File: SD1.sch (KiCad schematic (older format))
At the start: 32 parts, among them J107 FPC PMS, Q101 BSS138, Q102 PDTC114EU,115, SW103 Multidirection_Switch, SW104 Multifunction_Switch, U101 TLV70233_SOT23-5, U102 ER-TFTM028-4, U104 CC2652P, U107 MCP23017

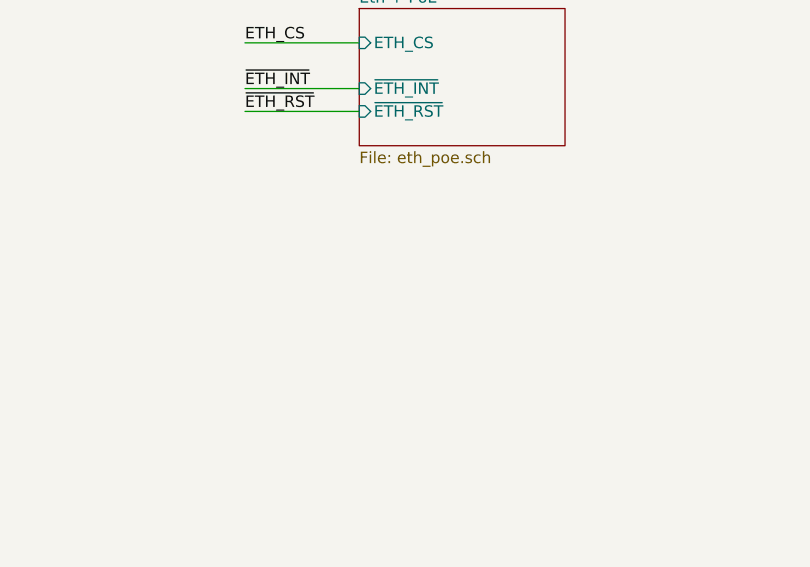
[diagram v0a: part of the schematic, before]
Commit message: Boilerplate for CO sensor
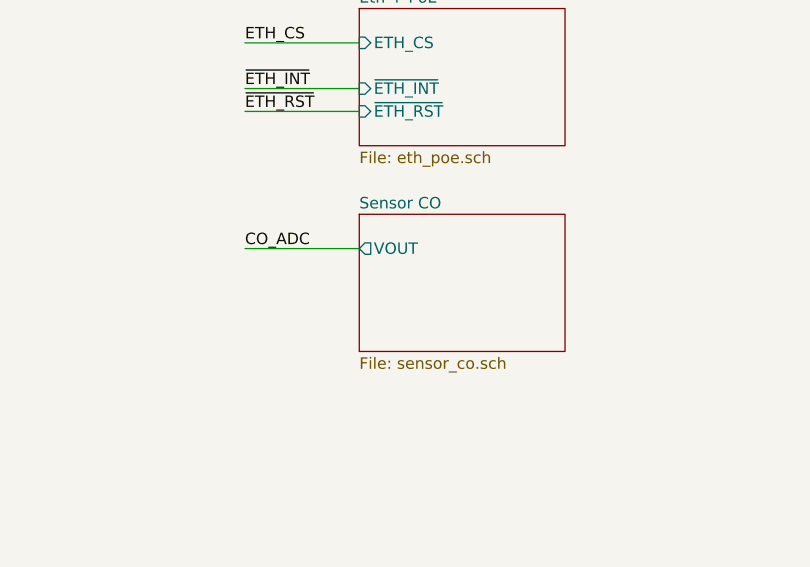
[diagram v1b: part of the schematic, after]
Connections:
- net labels added: CO_ADC
- wire segments 130 -> 131
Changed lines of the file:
@@
 $Descr A3 16535 11693
 encoding utf-8
-Sheet 1 4
+Sheet 1 5
 Title ""
 Date ""
@@
 I2C_SCL
 NoConn ~ 8700 7250
+Wire Wire Line
+	1000 5800 1500 5800
+Text Label 1000 5800 0    50   ~ 0
+CO_ADC
+$Sheet
+S 1500 5650 900  600
+U 5F98DBF7
+F0 "Sensor CO" 50
+F1 "sensor_co.sch" 50
+F2 "VOUT" O L 1500 5800 50
+$EndSheet
 $EndSCHEMATC

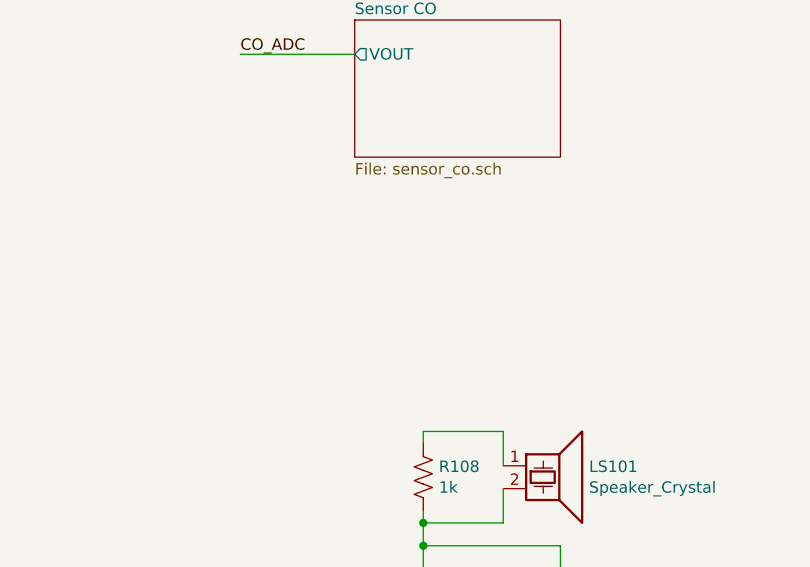
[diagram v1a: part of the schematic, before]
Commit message: Add VOC sensor
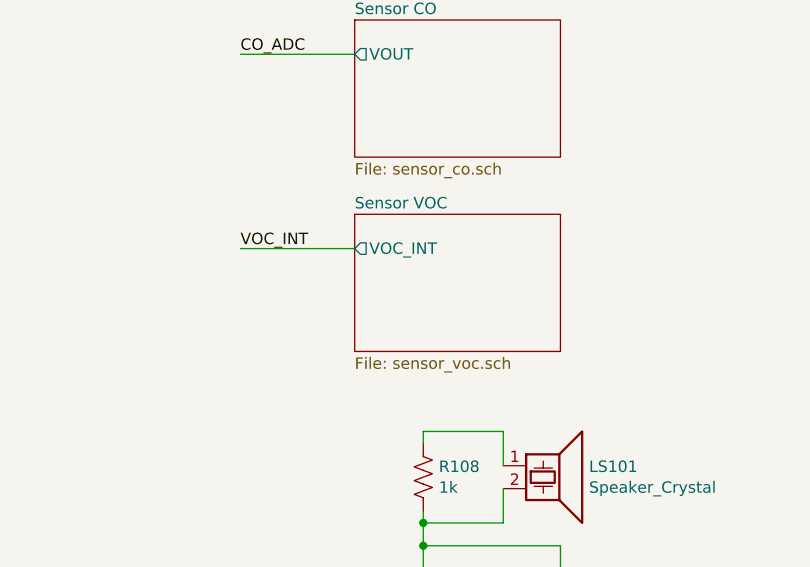
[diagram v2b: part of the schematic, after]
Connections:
- net labels added: VOC_INT
- wire segments 131 -> 132
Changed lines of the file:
@@
 $Descr A3 16535 11693
 encoding utf-8
-Sheet 1 5
+Sheet 1 6
 Title ""
 Date ""
@@
 CO_ADC
 $Sheet
+S 1500 6500 900  600
+U 5F97F9E8
+F0 "Sensor VOC" 50
+F1 "sensor_voc.sch" 50
+F2 "VOC_INT" O L 1500 6650 50
+$EndSheet
+$Sheet
 S 1500 5650 900  600
 U 5F98DBF7
@@
 F2 "VOUT" O L 1500 5800 50
 $EndSheet
+Wire Wire Line
+	1000 6650 1500 6650
+Text Label 1000 6650 0    50   ~ 0
+VOC_INT
 $EndSCHEMATC

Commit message: Added CO sensor
Carbon Monoxide Sensor layout
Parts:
- J107: symbol mylib:RECAPS_Master_r0 -> SD1-rescue:RECAPS_Master_r0-mylib
- SW103: symbol mylib:Multidirection_Switch -> SD1-rescue:Multidirection_Switch-mylib
- SW104: symbol mylib:Multifunction_Switch -> SD1-rescue:Multifunction_Switch-mylib
- U102: symbol mylib:ER-TFTM028-4 -> SD1-rescue:ER-TFTM028-4-mylib
- U104: symbol mylib:CC2652P -> SD1-rescue:CC2652P-mylib
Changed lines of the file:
@@
 $EndDescr
 $Comp
-L mylib:CC2652P U104
+L SD1-rescue:CC2652P-mylib U104
 U 1 1 5F5DA505
 P 7850 3300
@@
 $EndBitmap
 $Comp
-L mylib:Multifunction_Switch SW104
+L SD1-rescue:Multifunction_Switch-mylib SW104
 U 1 1 5F899D75
 P 5350 9300
@@
 	5650 9400 5700 9400
 $Comp
-L mylib:Multidirection_Switch SW103
+L SD1-rescue:Multidirection_Switch-mylib SW103
 U 1 1 5F978A8D
 P 3750 9300
@@
 SPKR
 $Comp
-L mylib:ER-TFTM028-4 U102
+L SD1-rescue:ER-TFTM028-4-mylib U102
 U 1 1 5F69622B
 P 12900 2700
@@
 $EndComp
 $Comp
-L mylib:ER-TFTM028-4 U102
+L SD1-rescue:ER-TFTM028-4-mylib U102
 U 2 1 5F6972E3
 P 15450 1450
@@
 NoConn ~ 7100 10700
 $Comp
-L mylib:RECAPS_Master_r0 J?
+L SD1-rescue:RECAPS_Master_r0-mylib J?
 U 1 1 5FAEBA7D
 P 7400 10250

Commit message: Minor cleanup
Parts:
- J107: symbol SD1-rescue:RECAPS_Master_r0-mylib -> mylib:RECAPS_Master_r0
- SW103: symbol SD1-rescue:Multidirection_Switch-mylib -> mylib:Multidirection_Switch
- SW104: symbol SD1-rescue:Multifunction_Switch-mylib -> mylib:Multifunction_Switch
- U102: symbol SD1-rescue:ER-TFTM028-4-mylib -> mylib:ER-TFTM028-4
- U104: symbol SD1-rescue:CC2652P-mylib -> mylib:CC2652P
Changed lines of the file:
@@
 $EndDescr
 $Comp
-L SD1-rescue:CC2652P-mylib U104
+L mylib:CC2652P U104
 U 1 1 5F5DA505
 P 7850 3300
@@
 $EndBitmap
 $Comp
-L SD1-rescue:Multifunction_Switch-mylib SW104
+L mylib:Multifunction_Switch SW104
 U 1 1 5F899D75
 P 5350 9300
@@
 	5650 9400 5700 9400
 $Comp
-L SD1-rescue:Multidirection_Switch-mylib SW103
+L mylib:Multidirection_Switch SW103
 U 1 1 5F978A8D
 P 3750 9300
@@
 SPKR
 $Comp
-L SD1-rescue:ER-TFTM028-4-mylib U102
+L mylib:ER-TFTM028-4 U102
 U 1 1 5F69622B
 P 12900 2700
@@
 $EndComp
 $Comp
-L SD1-rescue:ER-TFTM028-4-mylib U102
+L mylib:ER-TFTM028-4 U102
 U 2 1 5F6972E3
 P 15450 1450
@@
 NoConn ~ 7100 10700
 $Comp
-L SD1-rescue:RECAPS_Master_r0-mylib J?
+L mylib:RECAPS_Master_r0 J?
 U 1 1 5FAEBA7D
 P 7400 10250

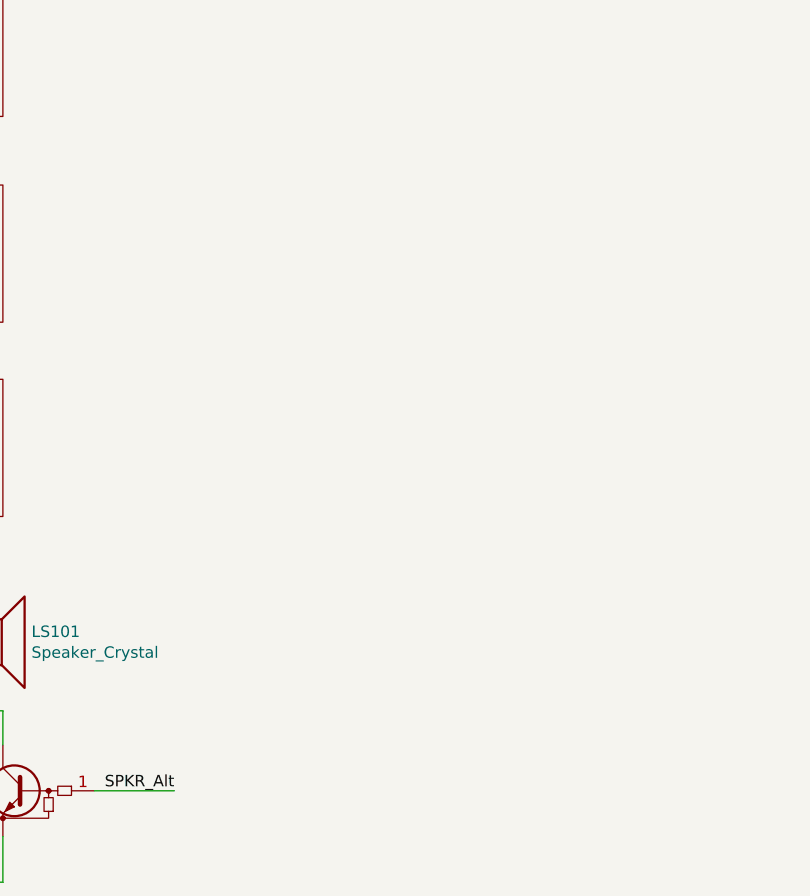
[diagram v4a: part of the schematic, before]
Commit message: Add PIR motion and sheet for smoke
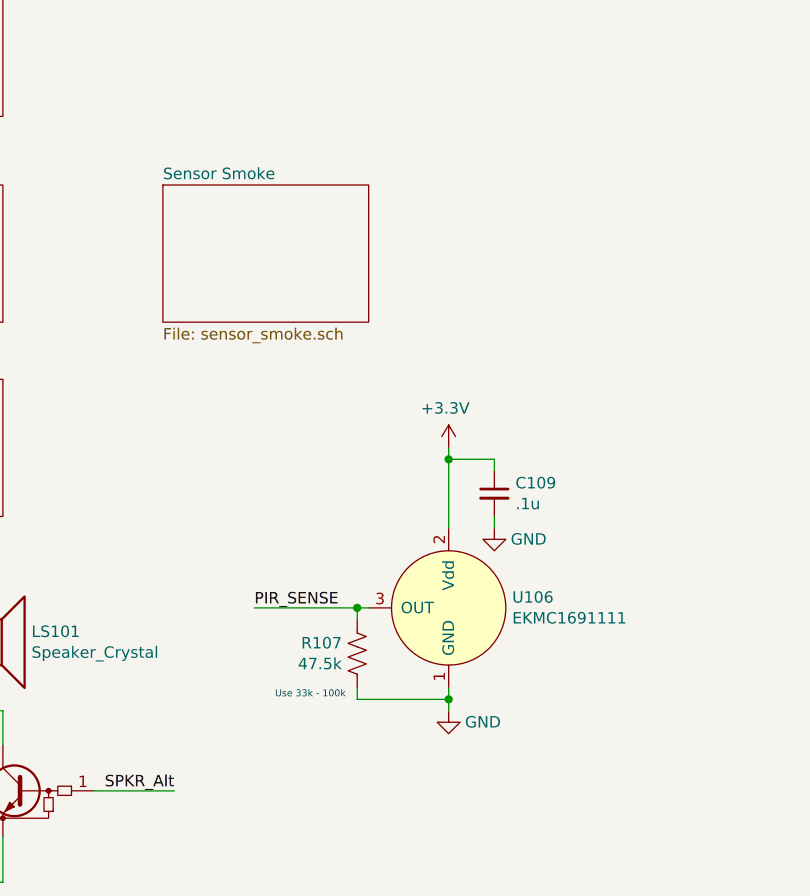
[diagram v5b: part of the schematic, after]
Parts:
- added C109: .1u, Capacitor_SMD:C_0402_1005Metric, symbol Device:C_Small
- added R107: 47.5k, Resistor_SMD:R_0603_1608Metric, symbol Device:R_US
- added U106: EKMC1691111, symbol mylib:EKMC1691111
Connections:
- net labels added: PIR_SENSE
- wire segments 132 -> 144
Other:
- note added: "Use 33k - 100k"
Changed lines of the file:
@@
 $Descr A3 16535 11693
 encoding utf-8
-Sheet 1 6
+Sheet 1 7
 Title ""
 Date ""
@@
 Text Label 1000 6650 0    50   ~ 0
 VOC_INT
+$Sheet
+S 3100 5650 900  600
+U 5F9DB5BA
+F0 "Sensor Smoke" 50
+F1 "sensor_smoke.sch" 50
+$EndSheet
+$Comp
+L mylib:EKMC1691111 U106
+U 1 1 5FA05437
+P 4350 7500
+F 0 "U106" H 4628 7546 50  0000 L CNN
+F 1 "EKMC1691111" H 4628 7455 50  0000 L CNN
+F 2 "" H 4350 6650 50  0001 C CNN
+F 3 "https://www3.panasonic.biz/ac/ae/search_num/index.jsp?c=detail&part_no=EKMC1691111" H 4350 6650 50  0001 C CNN
+F 4 "EKMC1691111" H 4350 7500 50  0001 C CNN "MPN"
+F 5 "255-6303-ND" H 4350 7500 50  0001 C CNN "Digikey"
+F 6 "Sensor PIR (Passive Infrared) 98.425\" (2.5m) - Module" H 4350 7500 50  0001 C CNN "Note"
+	1    4350 7500
+	1    0    0    -1
+$EndComp
+$Comp
+L power:+3.3V #PWR?
+U 1 1 5FA069F2
+P 4350 6800
+AR Path="/5E715318/5FA069F2" Ref="#PWR?"  Part="1"
+AR Path="/5FA069F2" Ref="#PWR0181"  Part="1"
+F 0 "#PWR0181" H 4350 6650 50  0001 C CNN
+F 1 "+3.3V" H 4365 6973 50  0000 C CNN
+F 2 "" H 4350 6800 50  0001 C CNN
+F 3 "" H 4350 6800 50  0001 C CNN
+	1    4350 6800
+	-1   0    0    -1
+$EndComp
+$Comp
+L Device:C_Small C?
+U 1 1 5FA0C8AA
+P 4550 7000
+AR Path="/5F98DBF7/5FA0C8AA" Ref="C?"  Part="1"
+AR Path="/5FA0C8AA" Ref="C109"  Part="1"
+F 0 "C109" H 4642 7046 50  0000 L CNN
+F 1 ".1u" H 4642 6955 50  0000 L CNN
+F 2 "Capacitor_SMD:C_0402_1005Metric" H 4550 7000 50  0001 C CNN
+F 3 "~" H 4550 7000 50  0001 C CNN
+F 4 "311-1336-1-ND" H 4550 7000 50  0001 C CNN "Digikey"
+F 5 "10%" H 4550 7000 50  0001 C CNN "Error"
+F 6 "C129131" H 4550 7000 50  0001 C CNN "LCSC"
+F 7 "CC0402KRX5R6BB104" H 4550 7000 50  0001 C CNN "MPN"
+F 8 "CAP CER 0.1UF 10V X5R 0402" H 4550 7000 50  0001 C CNN "Note"
+	1    4550 7000
+	1    0    0    -1
+$EndComp
+Wire Wire Line
+	4550 6850 4350 6850
+Wire Wire Line
+	4350 6800 4350 6850
+Connection ~ 4350 6850
+Wire Wire Line
+	4350 6850 4350 7150
+Wire Wire Line
+	4550 6900 4550 6850
+$Comp
+L power:GND #PWR0182
+U 1 1 5FA287E8
+P 4550 7150
+F 0 "#PWR0182" H 4550 6900 50  0001 C CNN
+F 1 "GND" H 4700 7100 50  0000 C CNN
+F 2 "" H 4550 7150 50  0001 C CNN
+F 3 "" H 4550 7150 50  0001 C CNN
+	1    4550 7150
+	1    0    0    -1
+$EndComp
+Wire Wire Line
+	4550 7150 4550 7100
+$Comp
+L power:GND #PWR0183
+U 1 1 5FA3C76C
+P 4350 7950
+F 0 "#PWR0183" H 4350 7700 50  0001 C CNN
+F 1 "GND" H 4500 7900 50  0000 C CNN
+F 2 "" H 4350 7950 50  0001 C CNN
+F 3 "" H 4350 7950 50  0001 C CNN
+	1    4350 7950
+	1    0    0    -1
+$EndComp
+Wire Wire Line
+	4350 7900 4350 7850
+Wire Wire Line
+	3500 7500 3950 7500
+Text Label 3500 7500 0    50   ~ 0
+PIR_SENSE
+Wire Wire Line
+	3950 7850 3950 7900
+Wire Wire Line
+	3950 7900 4350 7900
+Connection ~ 4350 7900
+Wire Wire Line
+	4350 7950 4350 7900
+Wire Wire Line
+	3950 7550 3950 7500
+Connection ~ 3950 7500
+Wire Wire Line
+	3950 7500 4000 7500
+Text Notes 3900 7900 2    30   ~ 0
+Use 33k - 100k
+$Comp
+L Device:R_US R?
+U 1 1 5FAB260D
+P 3950 7700
+AR Path="/5FED2126/5FAB260D" Ref="R?"  Part="1"
+AR Path="/5FAB260D" Ref="R107"  Part="1"
+F 0 "R107" H 4017 7654 50  0000 L CNN
+F 1 "47.5k" H 4017 7745 50  0000 L CNN
+F 2 "Resistor_SMD:R_0603_1608Metric" H 3950 7700 60  0001 C CNN
+F 3 "" H 3950 7700 60  0001 C CNN
+	1    3950 7700
+	-1   0    0    1
+$EndComp
 $EndSCHEMATC

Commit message: Minor smoke cleanup
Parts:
- U106: footprint (none) -> mylib:EKM
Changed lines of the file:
@@
 F 0 "U106" H 4628 7546 50  0000 L CNN
 F 1 "EKMC1691111" H 4628 7455 50  0000 L CNN
-F 2 "" H 4350 6650 50  0001 C CNN
+F 2 "mylib:EKM" H 4350 6650 50  0001 C CNN
 F 3 "https://www3.panasonic.biz/ac/ae/search_num/index.jsp?c=detail&part_no=EKMC1691111" H 4350 6650 50  0001 C CNN
 F 4 "EKMC1691111" H 4350 7500 50  0001 C CNN "MPN"

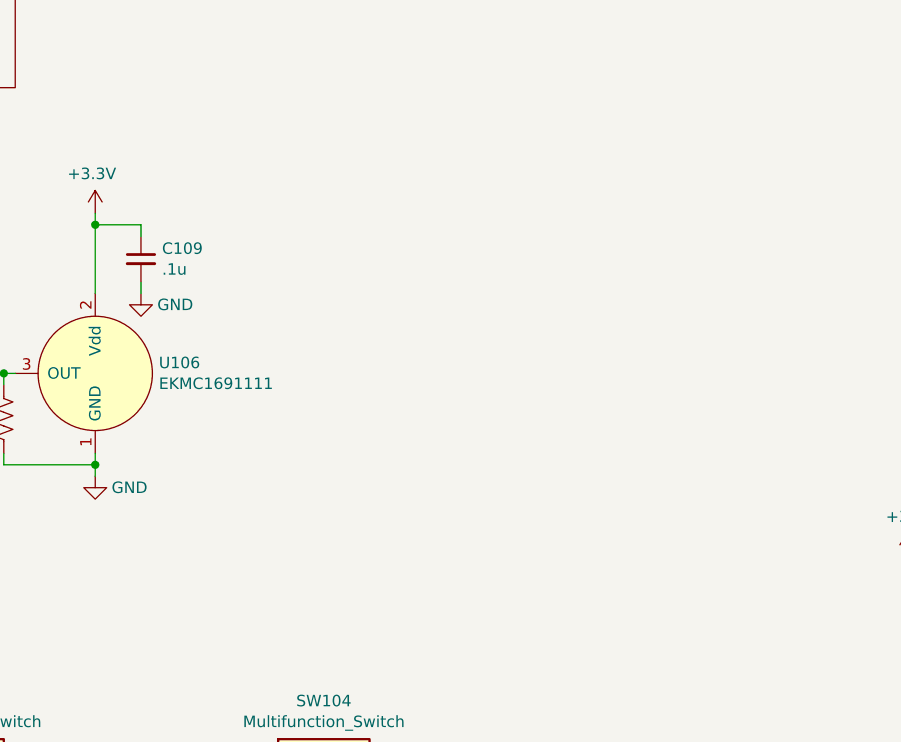
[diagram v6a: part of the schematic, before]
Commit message: Add SPS30 PMS sensor
-Fix cap
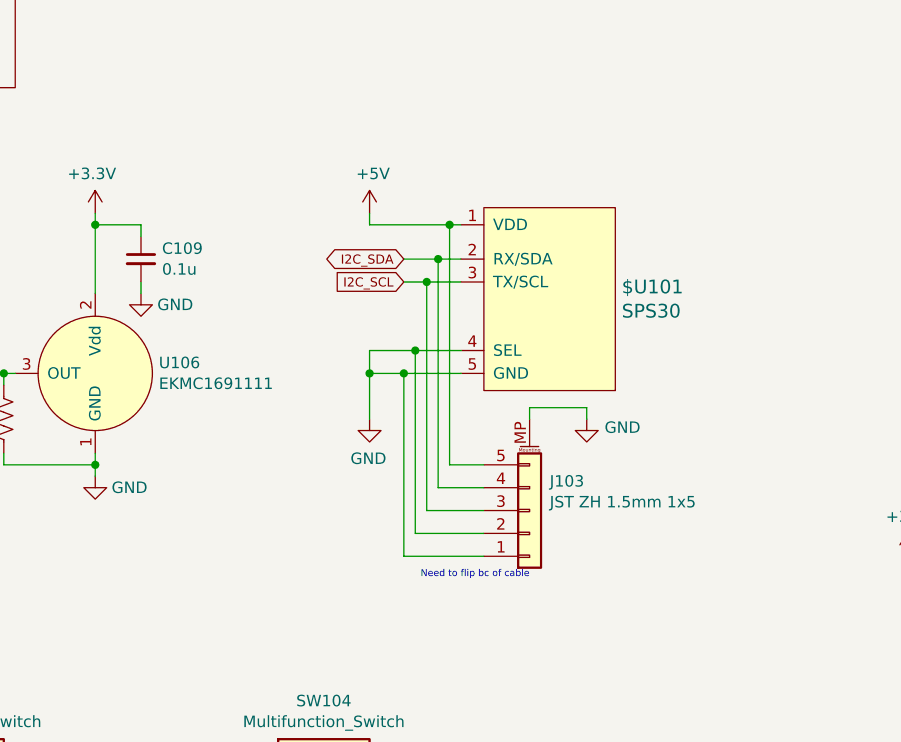
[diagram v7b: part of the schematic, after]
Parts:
- added $U101: SPS30, symbol mylib:SPS30
- added J103: JST ZH 1.5mm 1x5, mylib:JST-ZR-B5B-SM4-TFLFSN_1x05-1MP_P1.5mm_Vertical, symbol Connector_Generic_MountingPin:Conn_01x05_MountingPin
- C109: value .1u -> 0.1u; footprint Capacitor_SMD:C_0402_1005Metric -> Capacitor_SMD:C_0603_1608Metric; Digikey 311-1336-1-ND -> 1292-1643-1-ND; Error 10% -> (none); LCSC C129131 -> (none); MPN CC0402KRX5R6BB104 -> 0603B104K500CT; Note CAP CER 0.1UF 10V X5R 0402 -> CAP CER 0.1UF 50V X7R 0603
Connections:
- net labels added: +5V
- wire segments 144 -> 170
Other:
- note added: "Need to flip bc of cable"
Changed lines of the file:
@@
 	-1   0    0    -1
-$EndComp
-$Comp
-L Device:C_Small C?
-U 1 1 5FA0C8AA
-P 4550 7000
-AR Path="/5F98DBF7/5FA0C8AA" Ref="C?"  Part="1"
-AR Path="/5FA0C8AA" Ref="C109"  Part="1"
-F 0 "C109" H 4642 7046 50  0000 L CNN
-F 1 ".1u" H 4642 6955 50  0000 L CNN
-F 2 "Capacitor_SMD:C_0402_1005Metric" H 4550 7000 50  0001 C CNN
-F 3 "~" H 4550 7000 50  0001 C CNN
-F 4 "311-1336-1-ND" H 4550 7000 50  0001 C CNN "Digikey"
-F 5 "10%" H 4550 7000 50  0001 C CNN "Error"
-F 6 "C129131" H 4550 7000 50  0001 C CNN "LCSC"
-F 7 "CC0402KRX5R6BB104" H 4550 7000 50  0001 C CNN "MPN"
-F 8 "CAP CER 0.1UF 10V X5R 0402" H 4550 7000 50  0001 C CNN "Note"
-	1    4550 7000
-	1    0    0    -1
 $EndComp
 Wire Wire Line
@@
 	-1   0    0    1
 $EndComp
+$Comp
+L Device:C_Small C?
+U 1 1 5FAA8197
+P 4550 7000
+AR Path="/5E360A9B/5FAA8197" Ref="C?"  Part="1"
+AR Path="/5FAA8197" Ref="C109"  Part="1"
+AR Path="/5E49A000/5FAA8197" Ref="C?"  Part="1"
+AR Path="/5E5C8043/5E49A000/5FAA8197" Ref="C?"  Part="1"
+AR Path="/5E5C8043/5EAB3002/5FAA8197" Ref="C?"  Part="1"
+AR Path="/5E5C8043/5FAA8197" Ref="C?"  Part="1"
+AR Path="/5F9D72A5/5FAA8197" Ref="C?"  Part="1"
+AR Path="/5FCEDB09/5FAA8197" Ref="C?"  Part="1"
+F 0 "C109" H 4642 7046 50  0000 L CNN
+F 1 "0.1u" H 4642 6955 50  0000 L CNN
+F 2 "Capacitor_SMD:C_0603_1608Metric" H 4550 7000 50  0001 C CNN
+F 3 "~" H 4550 7000 50  0001 C CNN
+F 4 "0603B104K500CT" H 4550 7000 50  0001 C CNN "MPN"
+F 5 "1292-1643-1-ND" H 4550 7000 50  0001 C CNN "Digikey"
+F 6 "CAP CER 0.1UF 50V X7R 0603" H 4550 7000 50  0001 C CNN "Note"
+	1    4550 7000
+	1    0    0    -1
+$EndComp
+$Comp
+L mylib:SPS30 $U101
+U 1 1 5FC2D3DD
+P 6350 7150
+F 0 "$U101" H 6047 7178 60  0000 R CNN
+F 1 "SPS30" H 6047 7072 60  0000 R CNN
+F 2 "" V 6350 7150 60  0001 C CNN
+F 3 "" V 6625 7325 60  0001 C CNN
+F 4 "SPS30" H 6350 7150 50  0001 C CNN "MPN"
+F 5 "1649-1106-ND" H 6350 7150 50  0001 C CNN "Digikey"
+F 6 "PM2.5 PARTICLE SENSOR" H 6350 7150 50  0001 C CNN "Note"
+	1    6350 7150
+	-1   0    0    -1
+$EndComp
+Wire Wire Line
+	5950 7000 5850 7000
+Text GLabel 5700 7000 0    40   BiDi ~ 0
+I2C_SDA
+Text GLabel 5700 7100 0    40   Input ~ 0
+I2C_SCL
+Wire Wire Line
+	5950 7100 5800 7100
+Wire Wire Line
+	5950 6850 5900 6850
+$Comp
+L power:+5V #PWR0184
+U 1 1 5FC3EEC8
+P 5550 6800
+F 0 "#PWR0184" H 5550 6650 50  0001 C CNN
+F 1 "+5V" H 5565 6973 50  0000 C CNN
+F 2 "" H 5550 6800 50  0001 C CNN
+F 3 "" H 5550 6800 50  0001 C CNN
+	1    5550 6800
+	1    0    0    -1
+$EndComp
+Wire Wire Line
+	5550 6800 5550 6850
+Wire Wire Line
+	5950 7400 5750 7400
+Wire Wire Line
+	5550 7400 5550 7500
+Wire Wire Line
+	5550 7500 5700 7500
+$Comp
+L power:GND #PWR0185
+U 1 1 5FC59098
+P 5550 7700
+F 0 "#PWR0185" H 5550 7450 50  0001 C CNN
+F 1 "GND" H 5555 7527 50  0000 C CNN
+F 2 "" H 5550 7700 50  0001 C CNN
+F 3 "" H 5550 7700 50  0001 C CNN
+	1    5550 7700
+	-1   0    0    -1
+$EndComp
+Wire Wire Line
+	5550 7700 5550 7500
+Connection ~ 5550 7500
+$Comp
+L Connector_Generic_MountingPin:Conn_01x05_MountingPin J103
+U 1 1 5FC6B3E1
+P 6250 8100
+F 0 "J103" H 6338 7972 50  0000 L CNN
+F 1 "JST ZH 1.5mm 1x5" H 6338 8063 50  0000 L CNN
+F 2 "mylib:JST-ZR-B5B-SM4-TFLFSN_1x05-1MP_P1.5mm_Vertical" H 6250 8100 50  0001 C CNN
+F 3 "~" H 6250 8100 50  0001 C CNN
+F 4 "1.5mm 01x05 JST ZH" H 6250 8100 50  0001 C CNN "Note"
+	1    6250 8100
+	1    0    0    1
+$EndComp
+Wire Wire Line
+	5900 6850 5900 7900
+Wire Wire Line
+	5900 7900 6050 7900
+Connection ~ 5900 6850
+Wire Wire Line
+	5900 6850 5550 6850
+Wire Wire Line
+	5850 7000 5850 8000
+Wire Wire Line
+	5850 8000 6050 8000
+Connection ~ 5850 7000
+Wire Wire Line
+	5850 7000 5700 7000
+Wire Wire Line
+	5800 7100 5800 8100
+Wire Wire Line
+	5800 8100 6050 8100
+Connection ~ 5800 7100
+Wire Wire Line
+	5800 7100 5700 7100
+Wire Wire Line
+	5750 7400 5750 8200
+Wire Wire Line
+	5750 8200 6050 8200
+Connection ~ 5750 7400
+Wire Wire Line
+	5750 7400 5550 7400
+Wire Wire Line
+	6050 8300 5700 8300
+Wire Wire Line
+	5700 8300 5700 7500
+Connection ~ 5700 7500
+Wire Wire Line
+	5700 7500 5950 7500
+$Comp
+L power:GND #PWR0186
+U 1 1 5FCFB0A0
+P 6500 7700
+F 0 "#PWR0186" H 6500 7450 50  0001 C CNN
+F 1 "GND" H 6422 7663 50  0000 R CNN
+F 2 "" H 6500 7700 50  0001 C CNN
+F 3 "" H 6500 7700 50  0001 C CNN
+	1    6500 7700
+	-1   0    0    -1
+$EndComp
+Wire Wire Line
+	6250 7700 6250 7650
+Wire Wire Line
+	6250 7650 6500 7650
+Wire Wire Line
+	6500 7650 6500 7700
+Text Notes 6250 8400 2    30   ~ 0
+Need to flip bc of cable
 $EndSCHEMATC
